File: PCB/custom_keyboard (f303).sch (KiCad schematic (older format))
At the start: 366 parts, among them J1 Conn_01x04, J2 SM04B-SRSS-TB(LF)(SN), Q1 2N7002, SW1 SW_Push, U1 SRV05-4, U12 XC6206P332MR, U13 74LVC1G34, U14 STM32F303CBT6, X1 TestPoint_Small, X2 TestPoint_Small, Y2 8MHz

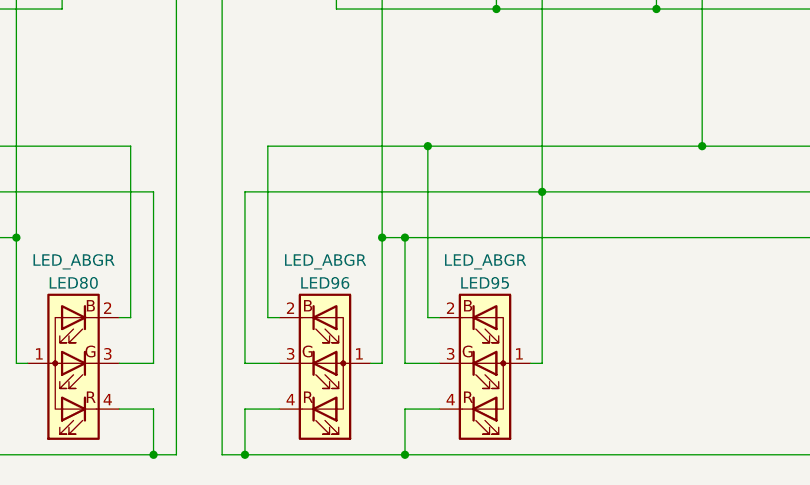
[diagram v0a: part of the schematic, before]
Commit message: Placed rest of LEDs onto board
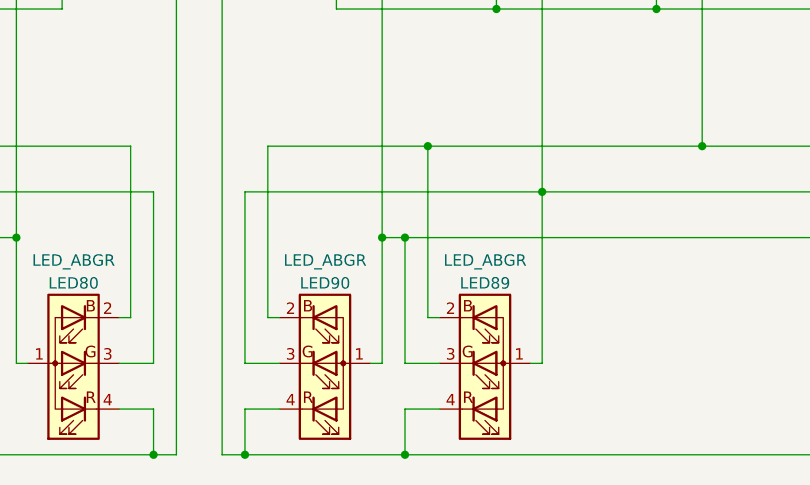
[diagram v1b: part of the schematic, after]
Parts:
- C2: LCSC Part (none) -> C1779
- I1, I2, I3: LCSC Part (none) -> C191206
- J2: LCSC Part (none) -> C160404
- LED1, LED10, LED11, LED12, LED13, LED14, LED15, LED16, LED17, LED18, LED19, LED2, LED20, LED21, LED22, LED23, LED24, LED25, LED26, LED27, LED28, LED29, LED3, LED30, LED31, LED32, LED33, LED34, LED35, LED36, LED37, LED38, LED39, LED4, LED40, LED41, LED42, LED43, LED44, LED45, LED46, LED47, LED48, LED49, LED5, LED50, LED51, LED52, LED53, LED54, LED55, LED56, LED57, LED58, LED59, LED6, LED60, LED61, LED62, LED63, LED64, LED65, LED66, LED67, LED68, LED69, LED7, LED70, LED71, LED72, LED73, LED74, LED75, LED76, LED77, LED78, LED79, LED8, LED80, LED81, LED82, LED83, LED84, LED85, LED86, LED87, LED88, LED9: LCSC Part (none) -> C409782
- LED89: renamed from LED95; LCSC Part (none) -> C409782
- LED90: renamed from LED96; LCSC Part (none) -> C409782
- Q1: LCSC Part (none) -> C8545
- R7: footprint Resistor_SMD:R_0805_2012Metric -> Resistor_SMD:R_0603_1608Metric; LCSC Part (none) -> C25803
- SW1: LCSC Part (none) -> C318884

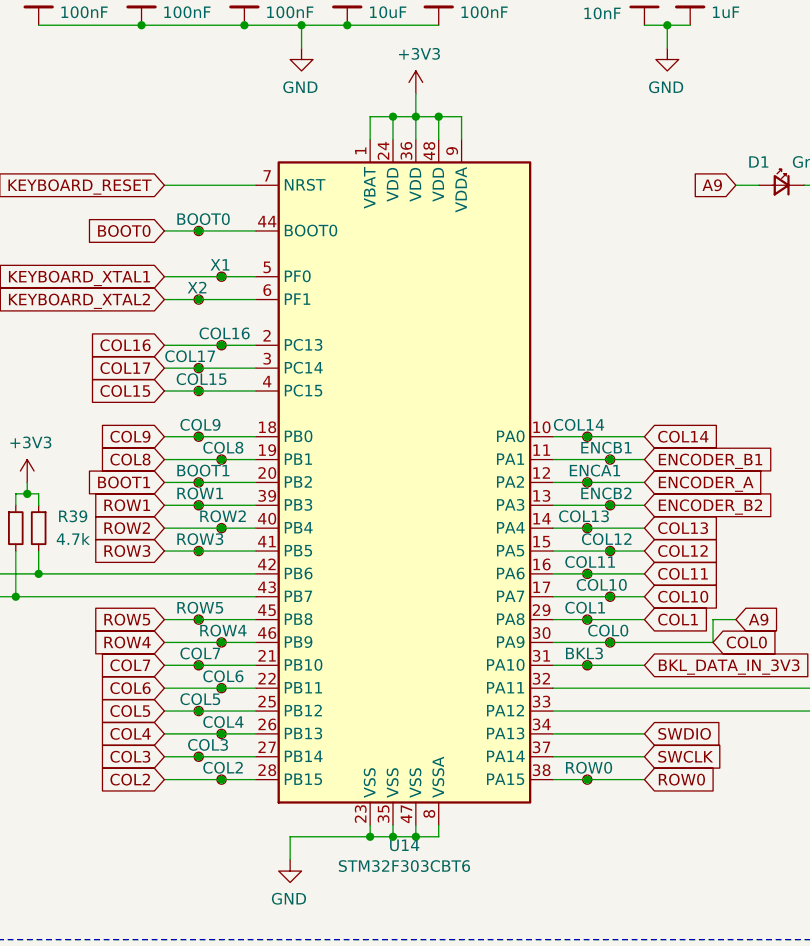
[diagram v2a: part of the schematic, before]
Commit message: Routed LEDs on I3
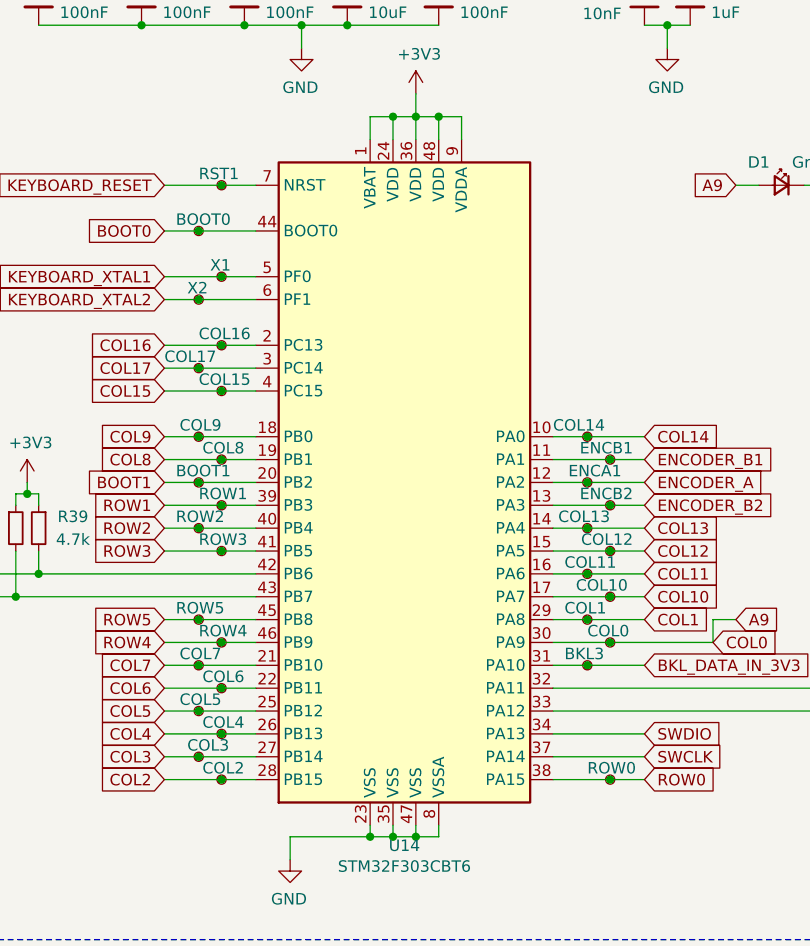
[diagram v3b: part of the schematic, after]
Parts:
- added RST1: TestPoint_Small, TestPoint:TestPoint_THTPad_D1.0mm_Drill0.5mm, symbol Connector:TestPoint_Small
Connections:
- net KEYBOARD_RESET: now also RST1.1
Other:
- moved on the sheet: COL15, ROW0, ROW1, ROW2, ROW3
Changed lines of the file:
@@
 L Connector:TestPoint_Small COL15
 U 1 1 93D3AF28
-P 4100 14500
-F 0 "COL15" H 4000 14550 50  0000 L CNN
-F 1 "TestPoint_Small" H 4148 14455 50  0001 L CNN
-F 2 "TestPoint:TestPoint_THTPad_D1.0mm_Drill0.5mm" H 4300 14500 50  0001 C CNN
-F 3 "~" H 4300 14500 50  0001 C CNN
-F 4 "0" H 4100 14500 50  0001 C CNN "JLCPCB BOM"
-	1    4100 14500
+P 4200 14500
+F 0 "COL15" H 4100 14550 50  0000 L CNN
+F 1 "TestPoint_Small" H 4248 14455 50  0001 L CNN
+F 2 "TestPoint:TestPoint_THTPad_D1.0mm_Drill0.5mm" H 4400 14500 50  0001 C CNN
+F 3 "~" H 4400 14500 50  0001 C CNN
+F 4 "0" H 4200 14500 50  0001 C CNN "JLCPCB BOM"
+	1    4200 14500
 	1    0    0    -1
 $EndComp
@@
 L Connector:TestPoint_Small ROW2
 U 1 1 93D3A9BC
-P 4200 15100
-F 0 "ROW2" H 4100 15050 50  0000 L CNN
-F 1 "TestPoint_Small" H 4248 15055 50  0001 L CNN
-F 2 "TestPoint:TestPoint_THTPad_D1.0mm_Drill0.5mm" H 4400 15100 50  0001 C CNN
-F 3 "~" H 4400 15100 50  0001 C CNN
-F 4 "0" H 4200 15100 50  0001 C CNN "JLCPCB BOM"
-	1    4200 15100
+P 4100 15100
+F 0 "ROW2" H 4000 15050 50  0000 L CNN
+F 1 "TestPoint_Small" H 4148 15055 50  0001 L CNN
+F 2 "TestPoint:TestPoint_THTPad_D1.0mm_Drill0.5mm" H 4300 15100 50  0001 C CNN
+F 3 "~" H 4300 15100 50  0001 C CNN
+F 4 "0" H 4100 15100 50  0001 C CNN "JLCPCB BOM"
+	1    4100 15100
 	1    0    0    1
 $EndComp
@@
 L Connector:TestPoint_Small ROW1
 U 1 1 93D3ABB4
-P 4100 15000
-F 0 "ROW1" H 4000 15050 50  0000 L CNN
-F 1 "TestPoint_Small" H 4148 14955 50  0001 L CNN
-F 2 "TestPoint:TestPoint_THTPad_D1.0mm_Drill0.5mm" H 4300 15000 50  0001 C CNN
-F 3 "~" H 4300 15000 50  0001 C CNN
-F 4 "0" H 4100 15000 50  0001 C CNN "JLCPCB BOM"
-	1    4100 15000
+P 4200 15000
+F 0 "ROW1" H 4100 15050 50  0000 L CNN
+F 1 "TestPoint_Small" H 4248 14955 50  0001 L CNN
+F 2 "TestPoint:TestPoint_THTPad_D1.0mm_Drill0.5mm" H 4400 15000 50  0001 C CNN
+F 3 "~" H 4400 15000 50  0001 C CNN
+F 4 "0" H 4200 15000 50  0001 C CNN "JLCPCB BOM"
+	1    4200 15000
 	1    0    0    -1
 $EndComp
@@
 	5650 15300 5800 15300
 Wire Wire Line
-	3950 13600 4350 13600
+	3950 13600 4200 13600
 $Comp
 L Device:C_Small C18
@@
 	12400 15350 12850 15350
 Wire Wire Line
-	3950 14700 4100 14700
-Connection ~ 4100 14700
-Wire Wire Line
 	4100 14700 4350 14700
 Wire Wire Line
@@
 	4200 15600 4350 15600
 Wire Wire Line
-	3950 14800 4200 14800
-Connection ~ 4200 14800
-Wire Wire Line
-	4200 14800 4350 14800
-Wire Wire Line
-	3950 14900 4100 14900
-Connection ~ 4100 14900
-Wire Wire Line
-	4100 14900 4350 14900
-Wire Wire Line
-	3950 14500 4100 14500
-Connection ~ 4100 14500
-Wire Wire Line
-	4100 14500 4350 14500
-Wire Wire Line
-	3950 15000 4100 15000
-Connection ~ 4100 15000
-Wire Wire Line
-	4100 15000 4350 15000
-Wire Wire Line
 	3950 15700 4100 15700
 Connection ~ 4100 15700
@@
 	4100 15700 4350 15700
 Wire Wire Line
-	3950 15100 4200 15100
-Connection ~ 4200 15100
-Wire Wire Line
-	4200 15100 4350 15100
+	3950 15100 4100 15100
 Connection ~ 4200 15800
 Wire Wire Line
@@
 Text GLabel 3950 14300 0    50   Input ~ 0
 COL16
-Wire Wire Line
-	5800 16200 5650 16200
-Connection ~ 5800 16200
-Wire Wire Line
-	6050 16200 5800 16200
 $Comp
 L Connector:TestPoint_Small ROW0
 U 1 1 93D3ADA4
-P 5800 16200
-F 0 "ROW0" H 5700 16250 50  0000 L CNN
-F 1 "TestPoint_Small" H 5848 16155 50  0001 L CNN
-F 2 "TestPoint:TestPoint_THTPad_D1.0mm_Drill0.5mm" H 6000 16200 50  0001 C CNN
-F 3 "~" H 6000 16200 50  0001 C CNN
-F 4 "0" H 5800 16200 50  0001 C CNN "JLCPCB BOM"
-	1    5800 16200
+P 5900 16200
+F 0 "ROW0" H 5800 16250 50  0000 L CNN
+F 1 "TestPoint_Small" H 5948 16155 50  0001 L CNN
+F 2 "TestPoint:TestPoint_THTPad_D1.0mm_Drill0.5mm" H 6100 16200 50  0001 C CNN
+F 3 "~" H 6100 16200 50  0001 C CNN
+F 4 "0" H 5900 16200 50  0001 C CNN "JLCPCB BOM"
+	1    5900 16200
 	1    0    0    -1
 $EndComp
@@
 L Connector:TestPoint_Small ROW3
 U 1 1 93D3A6FD
-P 4100 15200
-F 0 "ROW3" H 4000 15150 50  0000 L CNN
-F 1 "TestPoint_Small" H 4148 15155 50  0001 L CNN
-F 2 "TestPoint:TestPoint_THTPad_D1.0mm_Drill0.5mm" H 4300 15200 50  0001 C CNN
-F 3 "~" H 4300 15200 50  0001 C CNN
-F 4 "0" H 4100 15200 50  0001 C CNN "JLCPCB BOM"
-	1    4100 15200
+P 4200 15200
+F 0 "ROW3" H 4100 15150 50  0000 L CNN
+F 1 "TestPoint_Small" H 4248 15155 50  0001 L CNN
+F 2 "TestPoint:TestPoint_THTPad_D1.0mm_Drill0.5mm" H 4400 15200 50  0001 C CNN
+F 3 "~" H 4400 15200 50  0001 C CNN
+F 4 "0" H 4200 15200 50  0001 C CNN "JLCPCB BOM"
+	1    4200 15200
 	1    0    0    1
 $EndComp
 Text GLabel 3950 15200 0    50   Input ~ 0
 ROW3
-Wire Wire Line
-	3950 15200 4100 15200
-Connection ~ 4100 15200
-Wire Wire Line
-	4100 15200 4350 15200
 Text GLabel 3950 15000 0    50   Input ~ 0
 ROW1
@@
 	1    0    0    1
 $EndComp
+$Comp
+L Connector:TestPoint_Small RST1
+U 1 1 636EE336
+P 4200 13600
+F 0 "RST1" H 4100 13650 50  0000 L CNN
+F 1 "TestPoint_Small" H 4248 13555 50  0001 L CNN
+F 2 "TestPoint:TestPoint_THTPad_D1.0mm_Drill0.5mm" H 4400 13600 50  0001 C CNN
+F 3 "~" H 4400 13600 50  0001 C CNN
+F 4 "0" H 4200 13600 50  0001 C CNN "JLCPCB BOM"
+	1    4200 13600
+	1    0    0    -1
+$EndComp
+Connection ~ 4200 13600
+Wire Wire Line
+	4200 13600 4350 13600
+Connection ~ 4200 15200
+Wire Wire Line
+	4200 15200 4350 15200
+Wire Wire Line
+	3950 15200 4200 15200
+Connection ~ 4100 15100
+Wire Wire Line
+	4100 15100 4350 15100
+Wire Wire Line
+	3950 15000 4200 15000
+Connection ~ 4200 15000
+Wire Wire Line
+	4200 15000 4350 15000
+Wire Wire Line
+	3950 14900 4100 14900
+Connection ~ 4100 14900
+Wire Wire Line
+	4100 14900 4350 14900
+Wire Wire Line
+	3950 14800 4200 14800
+Connection ~ 4200 14800
+Wire Wire Line
+	4200 14800 4350 14800
+Wire Wire Line
+	3950 14700 4100 14700
+Connection ~ 4100 14700
+Wire Wire Line
+	3950 14500 4200 14500
+Connection ~ 4200 14500
+Wire Wire Line
+	4200 14500 4350 14500
+Wire Wire Line
+	5650 16200 5900 16200
+Connection ~ 5900 16200
+Wire Wire Line
+	5900 16200 6050 16200
 $EndSCHEMATC

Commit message: Gave JST connector its own fuse and ferrite bead
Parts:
- removed BKL5: TestPoint_Small, TestPoint:TestPoint_THTPad_D1.0mm_Drill0.5mm, symbol Connector:TestPoint_Small
- removed U13: 74LVC1G34, Package_TO_SOT_SMD:SOT-23-5, symbol 74xGxx:74LVC1G34
- added D5: Red, LED_SMD:LED_0805_2012Metric, symbol Device:LED_Small
- added F1: 500mA, Fuse:Fuse_1206_3216Metric, symbol Device:Polyfuse_Small
- added FB1: 60 @ 100 MHz, Inductor_SMD:L_0805_2012Metric, symbol Device:Ferrite_Bead_Small
- added J3: Conn_01x03, Connector_PinHeader_2.54mm:PinHeader_1x03_P2.54mm_Vertical, symbol Connector_Generic:Conn_01x03
- added R1: 680, Resistor_SMD:R_0805_2012Metric, symbol Device:R_Small
- R8: value 510 -> 680; LCSC Part C17734 -> C17798
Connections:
- net GND: now also J3.3 (Pin_3), R1.1
- net VBUS: now also F1.1; no longer FB15.2, J2.1 (Pin_1), U1.5 (VP)
- net VCC: now also J2.1 (Pin_1), D5.2 (A); no longer C10.1, C11.1, C12.1, C13.1, C43.1, C5.1, C6.1, I1.2 (VCC), I1.3 (SDB), I2.2 (VCC), I2.3 (SDB), I3.18 (AD), I3.2 (VCC), I3.3 (SDB), OL1.3 (VCC), U12.3 (VI)
- net at D2.1 (K): now also R1.2; no longer R8.2
- net BKL_DATA_IN_3V3 renamed A10
- net A10: now also J3.2 (Pin_2)
- new net: F1.2, FB1.1
- new net: D5.1 (K), R8.2
- new net +5V: C10.1, C11.1, C12.1, C13.1, C43.1, C5.1, C6.1, FB1.2, FB15.2, I1.2 (VCC), I1.3 (SDB), I2.2 (VCC), I2.3 (SDB), I3.18 (AD), I3.2 (VCC), I3.3 (SDB), J3.1 (Pin_1), OL1.3 (VCC), U1.5 (VP), U12.3 (VI)
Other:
- note added: "5V to 3V3"
- note added: "Crystal"
- note added: "JST Connection"
- note added: "OLED"
- note added: "Reset circuit"
- note added: "Rotary Encoders"
- note removed: "Keyboard 3.3v"
- note removed: "Keyboard Crystal"
- note removed: "Keyboard Encoders"
- note removed: "Keyboard OLED"
- note removed: "Keyboard Reset\n"
- note removed: "LED 3.3V to 5V"
- moved on the sheet: C18, C19, C20, C21, C22, C23, C24, C3, C43, C44, C7, D1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

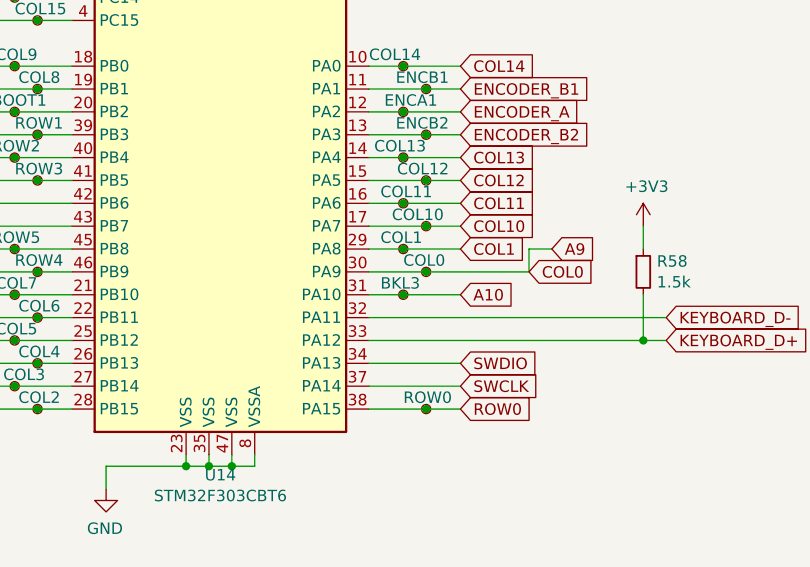
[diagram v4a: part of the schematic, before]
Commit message: Tweaked routing and footprints
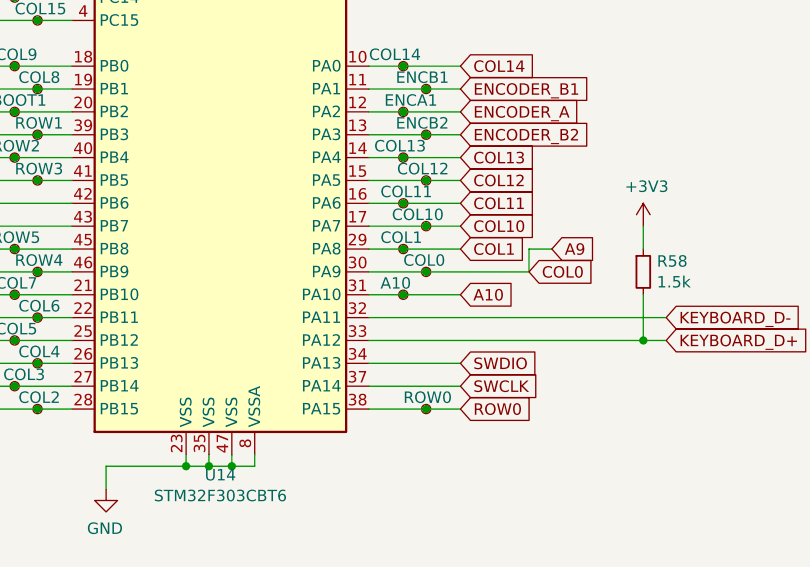
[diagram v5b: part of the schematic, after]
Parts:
- MX1, MX10, MX11, MX12, MX13, MX14, MX15, MX16, MX17, MX18, MX19, MX2, MX20, MX21, MX22, MX23, MX24, MX25, MX26, MX27, MX28, MX3, MX30, MX31, MX32, MX33, MX35, MX36, MX37, MX38, MX39, MX4, MX40, MX41, MX42, MX43, MX44, MX45, MX46, MX48, MX49, MX5, MX50, MX51, MX53, MX54, MX55, MX56, MX57, MX58, MX59, MX6, MX60, MX61, MX62, MX63, MX65, MX67, MX68, MX69, MX7, MX70, MX71, MX72, MX73, MX74, MX75, MX76, MX78, MX79, MX8, MX88, MX89, MX9, MX90: footprint MX_Only:MXOnly-1U-Hotswap -> custom-footprints:CherryMX_1.00u_PCB_KailhSocket
- MX29: footprint MX_Only:MXOnly-2U-Hotswap -> custom-footprints:CherryMX_2.00u_PCB_KailhSocket_StabWireBottom
- MX34, MX47: footprint MX_Only:MXOnly-1.5U-Hotswap -> custom-footprints:CherryMX_1.50u_PCB_KailhSocket
- MX52: footprint MX_Only:MXOnly-1.75U-Hotswap -> custom-footprints:CherryMX_1.75u_PCB_KailhSocket
- MX64, MX66: footprint MX_Only:MXOnly-2.25U-Hotswap -> custom-footprints:CherryMX_2.25u_PCB_KailhSocket_StabWireBottom
- MX77: footprint MX_Only:MXOnly-2.75U-Hotswap -> custom-footprints:CherryMX_2.75u_PCB_KailhSocket_StabWireBottom
- MX80, MX81, MX82, MX84, MX85, MX86, MX87: footprint MX_Only:MXOnly-1.25U-Hotswap -> custom-footprints:CherryMX_1.25u_PCB_KailhSocket
- MX83: footprint MX_Only:MXOnly-6.25U-Hotswap -> custom-footprints:CherryMX_6.25u_PCB_KailhSocket_StabWireBottom
- renumbered BKL3 to A10

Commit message: Exported for review
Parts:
- removed R18, R19: 20k, Resistor_SMD:R_0805_2012Metric, symbol Device:R_Small
- added C1, C8, C9: 100nF, Capacitor_SMD:C_0805_2012Metric, symbol Device:C_Small
- added LOGO1: QMK, custom-footprints:qmk, symbol Connector:TestPoint_Small
- added R15, R16: 20k, Resistor_SMD:R_0805_2012Metric, symbol Device:R_Small
- D1: LCSC Part C84256 -> C2297
- FB1, FB15, FB5: LCSC Part C337883 -> C18305
- J3: JLCPCB BOM (none) -> 0
- R11: LCSC Part C17798 -> C4328
- R5, R6: LCSC Part (none) -> C17414
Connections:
- net GND: now also C1.2, C8.2, C9.2, R15.1, R16.1
- net at I1.16 (C_FILT): now also C1.1
- net at I2.16 (C_FILT): now also C8.1
- net at I2.6 (R_EXT): now also R15.2
- net at I3.16 (C_FILT): now also C9.1
- net at I3.6 (R_EXT): now also R16.2
- no-connect marks 14 -> 12
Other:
- note added: "I1"
- note added: "I2"
- note added: "I3"
- note added: "RGB Matrix"
- moved on the sheet: A10, BOOT0, BOOT1, C10, C11, C12, C13, C18, C19, C2, C20, C21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
